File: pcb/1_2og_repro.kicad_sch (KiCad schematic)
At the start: 217 parts, among them J1 Pico EzMate, J2 USB_B_Mini, J3 Raw Header, J4 JST PH S3B, J5 Foam, SW1 MX_SW_solder, SW10 MX_SW_solder, SW11 MX_SW_solder, SW12 MX_SW_solder, SW13 MX_SW_solder, SW14 MX_SW_solder, SW15 MX_SW_solder, SW16 MX_SW_solder, SW17 MX_SW_solder, SW18 MX_SW_solder, SW19 MX_SW_solder, SW2 MX_SW_solder, SW20 MX_SW_solder, SW21 MX_SW_solder, SW22 MX_SW_solder, SW23 MX_SW_solder, SW24 MX_SW_solder, SW25 MX_SW_solder, SW26 MX_SW_solder, SW27 MX_SW_solder, SW28 MX_SW_solder, SW29 MX_SW_solder, SW3 MX_SW_solder, SW30 MX_SW_solder, SW31 MX_SW_solder, SW32 MX_SW_solder, SW33 MX_SW_solder, SW34 MX_SW_solder, SW35 MX_SW_solder, SW36 MX_SW_solder, SW37 MX_SW_solder, SW38 MX_SW_solder, SW39 MX_SW_solder, SW4 MX_SW_solder, SW40 MX_SW_solder, SW41 MX_SW_solder, SW42 MX_SW_solder, SW43 MX_SW_solder, SW44 MX_SW_solder, SW45 MX_SW_solder, SW46 MX_SW_solder, SW47 MX_SW_solder, SW48 MX_SW_solder, SW49 MX_SW_solder, SW5 MX_SW_solder, SW50 MX_SW_solder, SW51 MX_SW_solder, SW52 MX_SW_solder, SW53 MX_SW_solder, SW54 MX_SW_solder, SW55 MX_SW_solder, SW56 MX_SW_solder, SW57 MX_SW_solder, SW58 MX_SW_solder, SW59 MX_SW_solder, SW6 MX_SW_solder, SW60 MX_SW_solder, SW61 MX_SW_solder, SW62 MX_SW_solder, SW63 MX_SW_solder, SW64 MX_SW_solder, SW65 MX_SW_solder, SW66 MX_SW_solder, SW67 MX_SW_solder, SW68 MX_SW_solder, SW69 MX_SW_solder, SW7 MX_SW_solder, SW70 MX_SW_solder, SW71 MX_SW_solder, SW72 MX_SW_solder, SW73 MX_SW_solder, SW74 MX_SW_solder, SW75 MX_SW_solder, SW76 MX_SW_solder, SW77 MX_SW_solder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

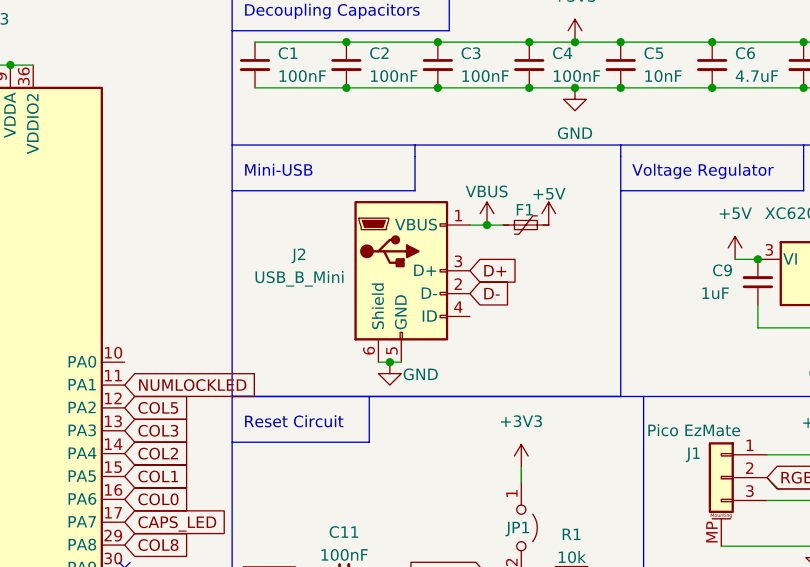
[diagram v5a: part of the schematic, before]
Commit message: fix usb pin symbol footpring mixup
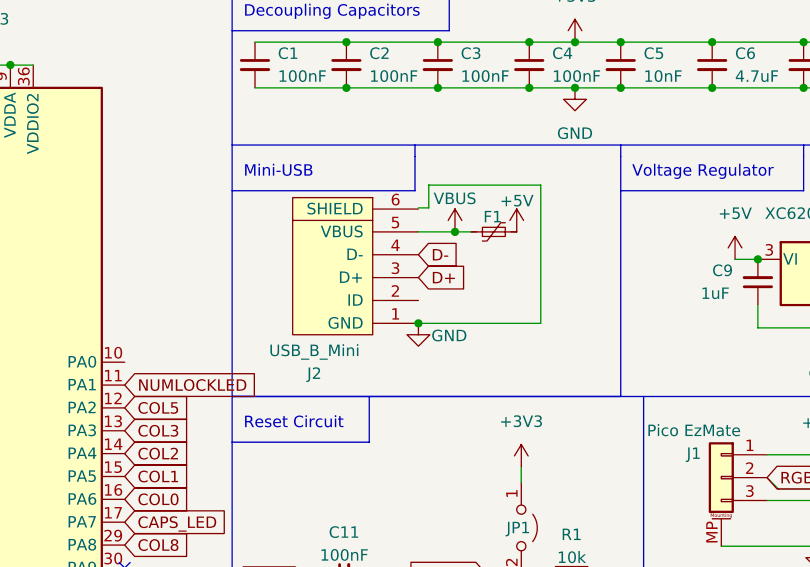
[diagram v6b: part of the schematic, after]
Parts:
- J2: symbol Connector:USB_B_Mini -> random-keyboard-parts:Molex-0548190519
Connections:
- net D-: now also J2.4 (D-); no longer J2.2 (D-)
- net GND: now also J2.1 (GND); no longer J2.5 (GND), J2.6 (Shield)
- net VBUS: now also J2.5 (VBUS); no longer J2.1 (VBUS)
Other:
- moved on the sheet: F1
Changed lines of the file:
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@@
   (junction (at 93.345 127.381) (diameter 0) (color 0 0 0 0)
   )
-  (junction (at 96.266 38.735) (diameter 0) (color 0 0 0 0)
-  )
   (junction (at 152.4 116.713) (diameter 0) (color 0 0 0 0)
   )
@@
   (junction (at 196.85 92.837) (diameter 0) (color 0 0 0 0)
   )
+  (junction (at 92.71 39.497) (diameter 0) (color 0 0 0 0)
+  )
   (junction (at 139.7 93.853) (diameter 0) (color 0 0 0 0)
   )
@@
   (junction (at 158.75 92.837) (diameter 0) (color 0 0 0 0)
   )
-  (junction (at 85.471 53.975) (diameter 0) (color 0 0 0 0)
-  )
   (junction (at 219.71 142.113) (diameter 0) (color 0 0 0 0)
   )
@@
   (junction (at 184.15 131.953) (diameter 0) (color 0 0 0 0)
   )
+  (junction (at 88.646 49.657) (diameter 0) (color 0 0 0 0)
+  )
   (junction (at 40.767 20.955) (diameter 0) (color 0 0 0 0)
   )
@@
     (stroke (width 0) (type default))
   )
-  (wire (pts (xy 84.201 53.975) (xy 85.471 53.975))
-    (stroke (width 0) (type default))
-  )
   (polyline (pts (xy 156.845 12.065) (xy 156.845 29.845))
     (stroke (width 0) (type default))
@@
     (stroke (width 0) (type default))
   )
+  (wire (pts (xy 89.789 34.29) (xy 102.235 34.29))
+    (stroke (width 0) (type default))
+  )
   (wire (pts (xy 144.78 92.837) (xy 152.4 92.837))
     (stroke (width 0) (type default))
@@
     (stroke (width 0) (type default))
   )
-  (wire (pts (xy 96.266 38.735) (xy 98.044 38.735))
+  (wire (pts (xy 92.71 39.497) (xy 94.488 39.497))
     (stroke (width 0) (type default))
   )
@@
     (stroke (width 0) (type default))
   )
+  (wire (pts (xy 88.646 36.83) (xy 89.789 36.83))
+    (stroke (width 0) (type default))
+  )
   (wire (pts (xy 204.47 92.837) (xy 212.09 92.837))
     (stroke (width 0) (type default))
@@
     (stroke (width 0) (type default))
   )
+  (wire (pts (xy 89.789 36.83) (xy 89.789 34.29))
+    (stroke (width 0) (type default))
+  )
   (wire (pts (xy 238.76 144.653) (xy 238.76 163.703))
     (stroke (width 0) (type default))
@@
     (stroke (width 0) (type default))
   )
-  (wire (pts (xy 86.741 53.975) (xy 85.471 53.975))
-    (stroke (width 0) (type default))
-  )
   (wire (pts (xy 139.7 82.677) (xy 139.7 93.853))
     (stroke (width 0) (type default))
@@
     (stroke (width 0) (type default))
   )
+  (wire (pts (xy 102.235 49.657) (xy 88.646 49.657))
+    (stroke (width 0) (type default))
+  )
   (polyline (pts (xy 198.755 12.065) (xy 156.845 12.065))
     (stroke (width 0) (type default))
@@
     (stroke (width 0) (type default))
   )
+  (wire (pts (xy 102.235 34.29) (xy 102.235 49.657))
+    (stroke (width 0) (type default))
+  )
   (wire (pts (xy 122.428 119.253) (xy 124.46 119.253))
     (stroke (width 0) (type default))
@@
     (stroke (width 0) (type default))
   )
-  (wire (pts (xy 94.361 38.735) (xy 96.266 38.735))
+  (wire (pts (xy 88.646 39.497) (xy 92.71 39.497))
     (stroke (width 0) (type default))
   )
@@
     )
   )
-  (global_label "D-" (shape input) (at 94.361 46.355 0) (fields_autoplaced)
+  (global_label "D-" (shape input) (at 88.646 42.037 0) (fields_autoplaced)
     (effects (font (size 1.27 1.27)) (justify left))
-    (property "Intersheetrefs" "${INTERSHEET_REFS}" (at 99.6165 46.2756 0)
+    (property "Intersheetrefs" "${INTERSHEET_REFS}" (at 93.9015 41.9576 0)
       (effects (font (size 1.27 1.27)) (justify left) hide)
     )
   )
-  (global_label "D+" (shape input) (at 94.361 43.815 0) (fields_autoplaced)
+  (global_label "D+" (shape input) (at 88.646 44.577 0) (fields_autoplaced)
     (effects (font (size 1.27 1.27)) (justify left))
-    (property "Intersheetrefs" "${INTERSHEET_REFS}" (at 99.6165 43.8944 0)
+    (property "Intersheetrefs" "${INTERSHEET_REFS}" (at 93.9015 44.6564 0)
       (effects (font (size 1.27 1.27)) (justify left) hide)
     )
@@
     )
   )
-  (symbol (lib_id "Device:Polyfuse_Small") (at 100.584 38.735 90) (unit 1)
+  (symbol (lib_id "Device:Polyfuse_Small") (at 97.028 39.497 90) (unit 1)
     (in_bom yes) (on_board yes) (dnp no)
-    (property "Reference" "F1" (at 100.457 37.084 90)
+    (property "Reference" "F1" (at 96.901 37.846 90)
       (effects (font (size 1.27 1.27)))
     )
-    (property "Value" "500mA" (at 100.584 37.084 90)
+    (property "Value" "500mA" (at 97.028 37.846 90)
       (effects (font (size 1.27 1.27)) hide)
     )
-    (property "Footprint" "Fuse:Fuse_1206_3216Metric" (at 105.664 37.465 0)
+    (property "Footprint" "Fuse:Fuse_1206_3216Metric" (at 102.108 38.227 0)
       (effects (font (size 1.27 1.27)) (justify left) hide)
     )
-    (property "Datasheet" "~" (at 100.584 38.735 0)
+    (property "Datasheet" "~" (at 97.028 39.497 0)
       (effects (font (size 1.27 1.27)) hide)
     )
@@
     )
   )
-  (symbol (lib_id "power:VBUS") (at 96.266 38.735 0) (mirror y) (unit 1)
+  (symbol (lib_id "power:VBUS") (at 92.71 39.497 0) (unit 1)
     (in_bom yes) (on_board yes) (dnp no)
-    (property "Reference" "#PWR016" (at 96.266 42.545 0)
+    (property "Reference" "#PWR016" (at 92.71 43.307 0)
       (effects (font (size 1.27 1.27)) hide)
     )
-    (property "Value" "VBUS" (at 96.266 35.052 0)
+    (property "Value" "VBUS" (at 92.71 35.814 0)
       (effects (font (size 1.27 1.27)))
     )
-    (property "Footprint" "" (at 96.266 38.735 0)
+    (property "Footprint" "" (at 92.71 39.497 0)
       (effects (font (size 1.27 1.27)) hide)
     )
-    (property "Datasheet" "" (at 96.266 38.735 0)
+    (property "Datasheet" "" (at 92.71 39.497 0)
       (effects (font (size 1.27 1.27)) hide)
     )
@@
     )
   )
-  (symbol (lib_id "Connector:USB_B_Mini") (at 86.741 43.815 0) (unit 1)
+  (symbol (lib_id "random-keyboard-parts:Molex-0548190519") (at 81.026 44.577 90) (unit 1)
     (in_bom yes) (on_board yes) (dnp no)
-    (property "Reference" "J2" (at 75.438 42.037 0)
+    (property "Reference" "J2" (at 77.089 55.245 90)
       (effects (font (size 1.27 1.27)))
     )
-    (property "Value" "USB_B_Mini" (at 75.438 44.577 0)
+    (property "Value" "USB_B_Mini" (at 77.089 52.705 90)
       (effects (font (size 1.27 1.27)))
     )
-    (property "Footprint" "random-keyboard-parts:Molex-0548190589" (at 90.551 45.085 0)
-      (effects (font (size 1.27 1.27)) hide)
+    (property "Footprint" "random-keyboard-parts:Molex-0548190589" (at 81.026 44.577 0)
+      (effects (font (size 1.524 1.524)) hide)
     )
-    (property "Datasheet" "~" (at 90.551 45.085 0)
-      (effects (font (size 1.27 1.27)) hide)
+    (property "Datasheet" "~" (at 81.026 44.577 0)
+      (effects (font (size 1.524 1.524)) hide)
     )
     (pin "1")
@@
     )
   )
-  (symbol (lib_name "+5V_1") (lib_id "power:+5V") (at 103.124 38.735 0) (mirror y) (unit 1)
+  (symbol (lib_name "+5V_1") (lib_id "power:+5V") (at 99.568 39.497 0) (mirror y) (unit 1)
     (in_bom yes) (on_board yes) (dnp no)
-    (property "Reference" "#PWR05" (at 103.124 42.545 0)
+    (property "Reference" "#PWR05" (at 99.568 43.307 0)
       (effects (font (size 1.27 1.27)) hide)
     )
-    (property "Value" "+5V" (at 103.124 35.306 0)
+    (property "Value" "+5V" (at 99.568 36.068 0)
       (effects (font (size 1.27 1.27)))
     )
-    (property "Footprint" "" (at 103.124 38.735 0)
+    (property "Footprint" "" (at 99.568 39.497 0)
       (effects (font (size 1.27 1.27)) hide)
     )
-    (property "Datasheet" "" (at 103.124 38.735 0)
+    (property "Datasheet" "" (at 99.568 39.497 0)
       (effects (font (size 1.27 1.27)) hide)
     )
@@
     )
   )
-  (symbol (lib_name "GND_2") (lib_id "power:GND") (at 85.471 53.975 0) (unit 1)
+  (symbol (lib_name "GND_2") (lib_id "power:GND") (at 88.646 49.657 0) (unit 1)
     (in_bom yes) (on_board yes) (dnp no)
-    (property "Reference" "#PWR09" (at 85.471 60.325 0)
+    (property "Reference" "#PWR09" (at 88.646 56.007 0)
       (effects (font (size 1.27 1.27)) hide)
     )
-    (property "Value" "GND" (at 88.9 55.372 0)
+    (property "Value" "GND" (at 92.075 51.054 0)
       (effects (font (size 1.27 1.27)))
     )
-    (property "Footprint" "" (at 85.471 53.975 0)
+    (property "Footprint" "" (at 88.646 49.657 0)
       (effects (font (size 1.27 1.27)) hide)
     )
-    (property "Datasheet" "" (at 85.471 53.975 0)
+    (property "Datasheet" "" (at 88.646 49.657 0)
       (effects (font (size 1.27 1.27)) hide)
     )

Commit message: add 6u support (firmware does not reflect this yet), usb 0548190519
previous USB is annoying to hand-solder without wick, using through-hole
pins may be less of a pain. 6u support is added because I miss my HHKB.
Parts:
- added D93: D_Small, Diode_SMD:D_SOD-123, symbol Device:D_Small
- added S6: MX_stab, marbastlib-mx:STAB_MX_6u, symbol marbastlib-mx:MX_stab
- added SW92, SW94: MX_SW_solder, marbastlib-mx:SW_MX_1u, symbol marbastlib-mx:MX_SW_solder
- added SW93: MX_SW_solder, marbastlib-mx:SW_MX_1.5u, symbol marbastlib-mx:MX_SW_solder
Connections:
- net COL10: now also SW94.2
- net COL6: now also SW92.2
- net COL9: now also SW93.1
- net GND: now also J2.6 (SHIELD)
- net ROW5: now also D93.1 (K)
- net at D82.2 (A), SW85.2: now also SW92.1
- net at D83.2 (A), SW86.2: now also SW94.1
- new net: D93.2 (A), SW93.2
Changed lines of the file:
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@@
   (junction (at 226.06 119.253) (diameter 0) (color 0 0 0 0)
   )
+  (junction (at 191.77 144.653) (diameter 0) (color 0 0 0 0)
+  )
   (junction (at 137.16 154.813) (diameter 0) (color 0 0 0 0)
   )
+  (junction (at 173.99 149.733) (diameter 0) (color 0 0 0 0)
+  )
   (junction (at 139.7 106.553) (diameter 0) (color 0 0 0 0)
   )
@@
   (junction (at 129.54 116.713) (diameter 0) (color 0 0 0 0)
   )
+  (junction (at 204.47 149.733) (diameter 0) (color 0 0 0 0)
+  )
   (junction (at 176.53 106.553) (diameter 0) (color 0 0 0 0)
   )
@@
   (junction (at 133.985 50.165) (diameter 0) (color 0 0 0 0)
   )
+  (junction (at 196.85 154.813) (diameter 0) (color 0 0 0 0)
+  )
   (junction (at 231.14 142.113) (diameter 0) (color 0 0 0 0)
   )
@@
     (stroke (width 0) (type default))
   )
+  (wire (pts (xy 203.327 149.733) (xy 204.47 149.733))
+    (stroke (width 0) (type default))
+  )
   (wire (pts (xy 173.99 104.013) (xy 181.61 104.013))
     (stroke (width 0) (type default))
@@
     (stroke (width 0) (type default))
   )
+  (wire (pts (xy 167.513 144.653) (xy 168.91 144.653))
+    (stroke (width 0) (type default))
+  )
   (polyline (pts (xy 156.845 12.065) (xy 156.845 29.845))
     (stroke (width 0) (type default))
@@
     (stroke (width 0) (type default))
   )
+  (wire (pts (xy 88.646 36.957) (xy 89.789 36.957))
+    (stroke (width 0) (type default))
+  )
   (wire (pts (xy 168.91 106.553) (xy 168.91 119.253))
     (stroke (width 0) (type default))
@@
     (stroke (width 0) (type default))
   )
-  (wire (pts (xy 204.47 154.813) (xy 173.99 154.813))
+  (wire (pts (xy 204.47 154.813) (xy 196.85 154.813))
     (stroke (width 0) (type default))
   )
@@
     (stroke (width 0) (type default))
   )
-  (wire (pts (xy 88.646 36.83) (xy 89.789 36.83))
-    (stroke (width 0) (type default))
-  )
   (wire (pts (xy 204.47 92.837) (xy 212.09 92.837))
     (stroke (width 0) (type default))
@@
     (stroke (width 0) (type default))
   )
-  (wire (pts (xy 89.789 36.83) (xy 89.789 34.29))
+  (wire (pts (xy 89.789 34.29) (xy 89.789 36.957))
     (stroke (width 0) (type default))
   )
@@
     (stroke (width 0) (type default))
   )
+  (wire (pts (xy 191.77 144.653) (xy 191.77 163.703))
+    (stroke (width 0) (type default))
+  )
   (wire (pts (xy 124.46 131.953) (xy 124.46 144.653))
     (stroke (width 0) (type default))
   )
-  (wire (pts (xy 191.77 131.953) (xy 191.77 163.703))
+  (wire (pts (xy 191.77 131.953) (xy 191.77 144.653))
     (stroke (width 0) (type default))
   )
@@
     (stroke (width 0) (type default))
   )
+  (wire (pts (xy 196.85 154.813) (xy 173.99 154.813))
+    (stroke (width 0) (type default))
+  )
   (wire (pts (xy 100.965 23.495) (xy 106.045 23.495))
     (stroke (width 0) (type default))
@@
     (stroke (width 0) (type default))
   )
+  (wire (pts (xy 198.247 144.653) (xy 199.39 144.653))
+    (stroke (width 0) (type default))
+  )
   (wire (pts (xy 196.85 104.013) (xy 204.47 104.013))
     (stroke (width 0) (type default))
@@
     (stroke (width 0) (type default))
   )
+  (wire (pts (xy 172.593 149.733) (xy 173.99 149.733))
+    (stroke (width 0) (type default))
+  )
   (wire (pts (xy 147.32 119.253) (xy 147.32 131.953))
     (stroke (width 0) (type default))
@@
     )
   )
+  (symbol (lib_id "marbastlib-mx:MX_SW_solder") (at 200.787 147.193 180) (unit 1)
+    (in_bom yes) (on_board yes) (dnp no)
+    (property "Reference" "SW94" (at 200.787 149.733 0)
+      (effects (font (size 1.27 1.27)))
+    )
+    (property "Value" "MX_SW_solder" (at 200.787 151.003 0)
+      (effects (font (size 1.27 1.27)) hide)
+    )
+    (property "Footprint" "marbastlib-mx:SW_MX_1u" (at 200.787 147.193 0)
+      (effects (font (size 1.27 1.27)) hide)
+    )
+    (property "Datasheet" "~" (at 200.787 147.193 0)
+      (effects (font (size 1.27 1.27)) hide)
+    )
+    (pin "1")
+    (pin "2")
+    (instances
+      (project "1_2og_repro"
+        (path "/70139223-fff4-476d-a728-a7aa752fc36c"
+          (reference "SW94") (unit 1)
+        )
+      )
+      (project "1_2_frl"
+        (path "/a8274e21-5f6e-4c7e-bbe0-133d7f65afea"
+          (reference "SW66") (unit 1)
+        )
+      )
+    )
+  )
   (symbol (lib_id "Device:D_Small") (at 137.16 101.473 90) (unit 1)
     (in_bom yes) (on_board yes) (dnp no)
@@
     )
   )
+  (symbol (lib_id "marbastlib-mx:MX_SW_solder") (at 170.053 147.193 180) (unit 1)
+    (in_bom yes) (on_board yes) (dnp no)
+    (property "Reference" "SW92" (at 170.053 149.733 0)
+      (effects (font (size 1.27 1.27)))
+    )
+    (property "Value" "MX_SW_solder" (at 170.053 151.003 0)
+      (effects (font (size 1.27 1.27)) hide)
+    )
+    (property "Footprint" "marbastlib-mx:SW_MX_1u" (at 170.053 147.193 0)
+      (effects (font (size 1.27 1.27)) hide)
+    )
+    (property "Datasheet" "~" (at 170.053 147.193 0)
+      (effects (font (size 1.27 1.27)) hide)
+    )
+    (pin "1")
+    (pin "2")
+    (instances
+      (project "1_2og_repro"
+        (path "/70139223-fff4-476d-a728-a7aa752fc36c"
+          (reference "SW92") (unit 1)
+        )
+      )
+      (project "1_2_frl"
+        (path "/a8274e21-5f6e-4c7e-bbe0-133d7f65afea"
+          (reference "SW65") (unit 1)
+        )
+      )
+    )
+  )
   (symbol (lib_id "power:VBUS") (at 178.435 17.653 0) (unit 1)
     (in_bom yes) (on_board yes) (dnp no) (fields_autoplaced)
@@
     )
   )
+  (symbol (lib_id "Device:D_Small") (at 196.85 152.273 90) (unit 1)
+    (in_bom yes) (on_board yes) (dnp no)
+    (property "Reference" "D93" (at 198.12 152.273 90)
+      (effects (font (size 1.27 1.27)) (justify right))
+    )
+    (property "Value" "D_Small" (at 199.39 154.178 90)
+      (effects (font (size 1.27 1.27)) (justify right) hide)
+    )
+    (property "Footprint" "Diode_SMD:D_SOD-123" (at 196.85 152.273 90)
+      (effects (font (size 1.27 1.27)) hide)
+    )
+    (property "Datasheet" "~" (at 196.85 152.273 90)
+      (effects (font (size 1.27 1.27)) hide)
+    )
+    (property "Sim.Device" "D" (at 196.85 152.273 0)
+      (effects (font (size 1.27 1.27)) hide)
+    )
+    (property "Sim.Pins" "1=K 2=A" (at 196.85 152.273 0)
+      (effects (font (size 1.27 1.27)) hide)
+    )
+    (pin "1")
+    (pin "2")
+    (instances
+      (project "1_2og_repro"
+        (path "/70139223-fff4-476d-a728-a7aa752fc36c"
+          (reference "D93") (unit 1)
+        )
+      )
+      (project "1_2_frl"
+        (path "/a8274e21-5f6e-4c7e-bbe0-133d7f65afea"
+          (reference "D57") (unit 1)
+        )
+      )
+    )
+  )
   (symbol (lib_id "Mechanical:MountingHole_Pad") (at 164.973 63.627 180) (unit 1)
     (in_bom yes) (on_board yes) (dnp no) (fields_autoplaced)
@@
     )
   )
+  (symbol (lib_id "marbastlib-mx:MX_SW_solder") (at 194.31 147.193 0) (unit 1)
+    (in_bom yes) (on_board yes) (dnp no)
+    (property "Reference" "SW93" (at 194.31 144.653 0)
+      (effects (font (size 1.27 1.27)))
+    )
+    (property "Value" "MX_SW_solder" (at 194.31 143.383 0)
+      (effects (font (size 1.27 1.27)) hide)
+    )
+    (property "Footprint" "marbastlib-mx:SW_MX_1.5u" (at 194.31 147.193 0)
+      (effects (font (size 1.27 1.27)) hide)
+    )
+    (property "Datasheet" "~" (at 194.31 147.193 0)
+      (effects (font (size 1.27 1.27)) hide)
+    )
+    (pin "1")
+    (pin "2")
+    (instances
+      (project "1_2og_repro"
+        (path "/70139223-fff4-476d-a728-a7aa752fc36c"
+          (reference "SW93") (unit 1)
+        )
+      )
+      (project "1_2_frl"
+        (path "/a8274e21-5f6e-4c7e-bbe0-133d7f65afea"
+          (reference "SW65") (unit 1)
+        )
+      )
+    )
+  )
   (symbol (lib_id "Device:C_Small") (at 141.605 20.955 0) (unit 1)
     (in_bom yes) (on_board yes) (dnp no) (fields_autoplaced)
@@
         )
       )
+    )
+  )
+  (symbol (lib_id "marbastlib-mx:MX_stab") (at 272.161 131.191 0) (unit 1)
+    (in_bom yes) (on_board yes) (dnp no) (fields_autoplaced)
+    (property "Reference" "S6" (at 278.511 130.429 0)
+      (effects (font (size 1.27 1.27)) (justify left))
+    )
+    (property "Value" "MX_stab" (at 278.511 132.969 0)
+      (effects (font (size 1.27 1.27)) (justify left))
+    )
+    (property "Footprint" "marbastlib-mx:STAB_MX_6u" (at 272.161 131.191 0)
+      (effects (font (size 1.27 1.27)) hide)
+    )
+    (property "Datasheet" "" (at 272.161 131.191 0)
+      (effects (font (size 1.27 1.27)) hide)
+    )
+    (instances
+      (project "1_2og_repro"
+        (path "/70139223-fff4-476d-a728-a7aa752fc36c"
+          (reference "S6") (unit 1)
+        )
+      )
